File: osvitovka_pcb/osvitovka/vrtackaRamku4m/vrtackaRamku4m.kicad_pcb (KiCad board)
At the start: 2 copper layers, 24 parts, among them J1 Screw_Terminal_01x01, J3 Screw_Terminal_01x01, J5 M+, J6 M-, Q1 BUZ11, SW1 SW_Push, U1 LM78M05_TO220, U2 LTV-817S

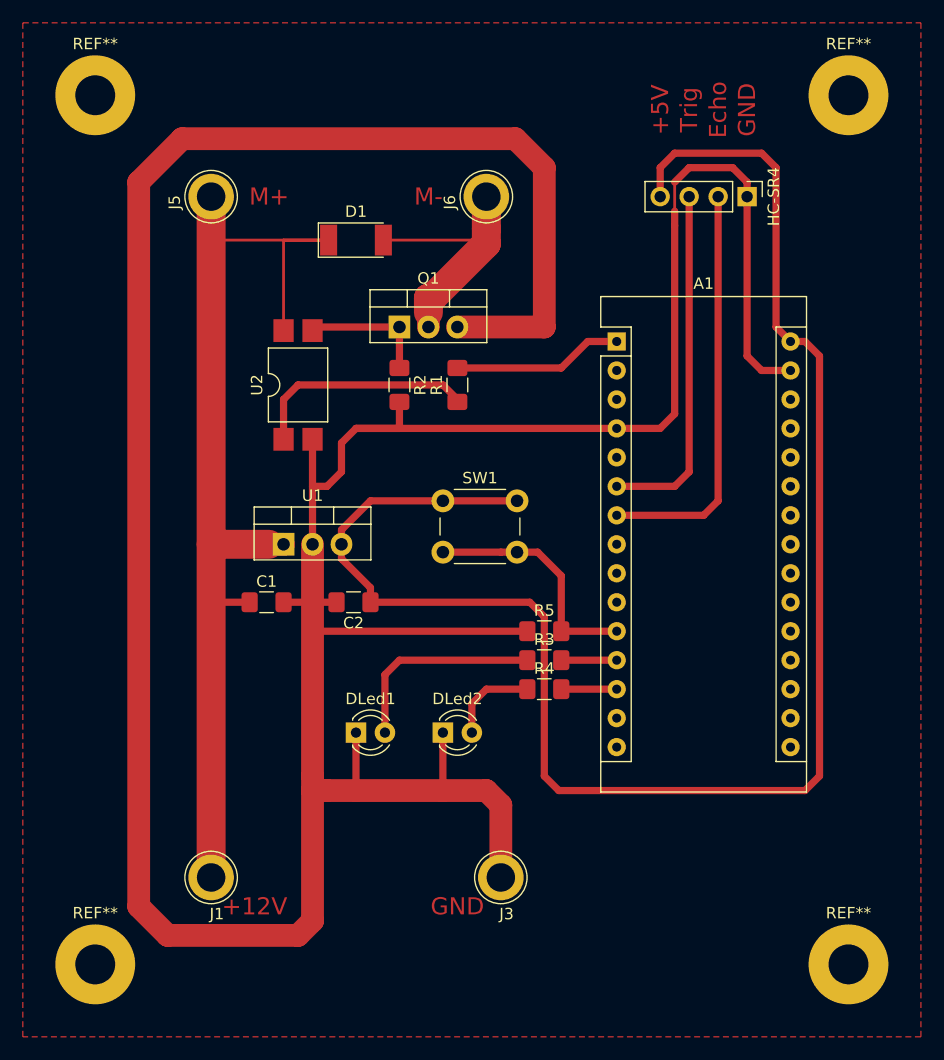
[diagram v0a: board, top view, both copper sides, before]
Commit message: Nová, zmenšená verze.
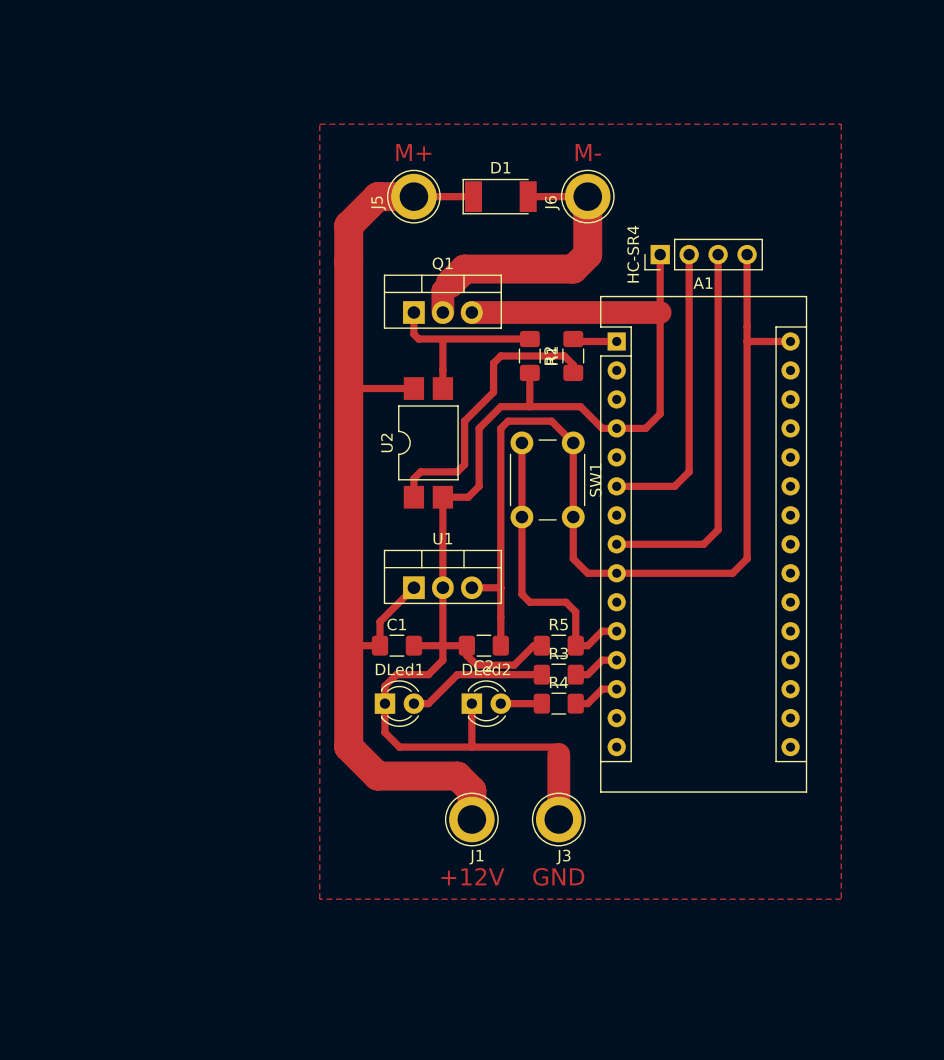
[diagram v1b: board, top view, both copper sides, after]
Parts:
- removed REF** (x4): MountingHole_3.5mm_Pad, MountingHole:MountingHole_3.5mm_Pad
- moved J1 23.4 mm to (141.0, 111.8)
- moved J5 17.8 mm to (135.9, 57.1)
- moved D1 13.3 mm to (143.5, 57.1)
- moved SW1 12.5 mm to (149.9, 78.7), turned to 270 degrees
- moved U2 12.5 mm to (137.2, 78.7)
- moved C1 12.0 mm to (134.4, 96.5)
- moved C2 12.0 mm to (142.0, 96.5)
- moved U1 12.0 mm to (135.9, 91.4)
- moved R2 11.7 mm to (146.1, 71.1)
- moved R1 10.5 mm to (149.9, 71.1)
- moved HC-SR4 9.16 mm to (157.5, 62.2), turned to 90 degrees
- moved J6 8.89 mm to (151.1, 57.1)
- moved J3 7.18 mm to (148.6, 111.8)
- moved DLed1 3.59 mm to (133.3, 101.6)
- moved DLed2 3.59 mm to (141.0, 101.6)
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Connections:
- A1 pad 29: GND -> Net-(A1-Pad29)
- A1 pad 6: Trig -> Echo
- A1 pad 7: Echo -> Net-(A1-Pad7)
- A1 pad 8: Net-(A1-Pad8) -> Trig
- A1 pad 9: Net-(A1-Pad9) -> +5V
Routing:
- net GND: track 354.0 -> 123.5 mm
- net +5V: track 148.2 -> 85.9 mm
- net +12V: track 151.3 -> 130.1 mm
- net PWM1: track 14.9 -> 3.90 mm
- net Echo: track 36.1 -> 25.9 mm
- net Net-(DLed1-Pad2): track 18.4 -> 12.6 mm
- net Net-(Q1-Pad1): track 11.3 -> 16.4 mm
- net Net-(R1-Pad1): track 20.0 -> 24.8 mm
- net Btn1: track 21.0 -> 25.7 mm
- net Net-(DLed2-Pad2): track 8.24 -> 3.90 mm
- net Trig: track 31.0 -> 33.5 mm
- net Net-(D1-Pad2): track 35.5 -> 33.1 mm
- net Led_yellow: track 4.86 -> 4.12 mm
- net Led_green: track 4.86 -> 4.12 mm
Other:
- board text removed: "+5V"
- board text removed: "Echo"
- board text removed: "Trig"

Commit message: Úprava PCB pro jednostranný plošňák.
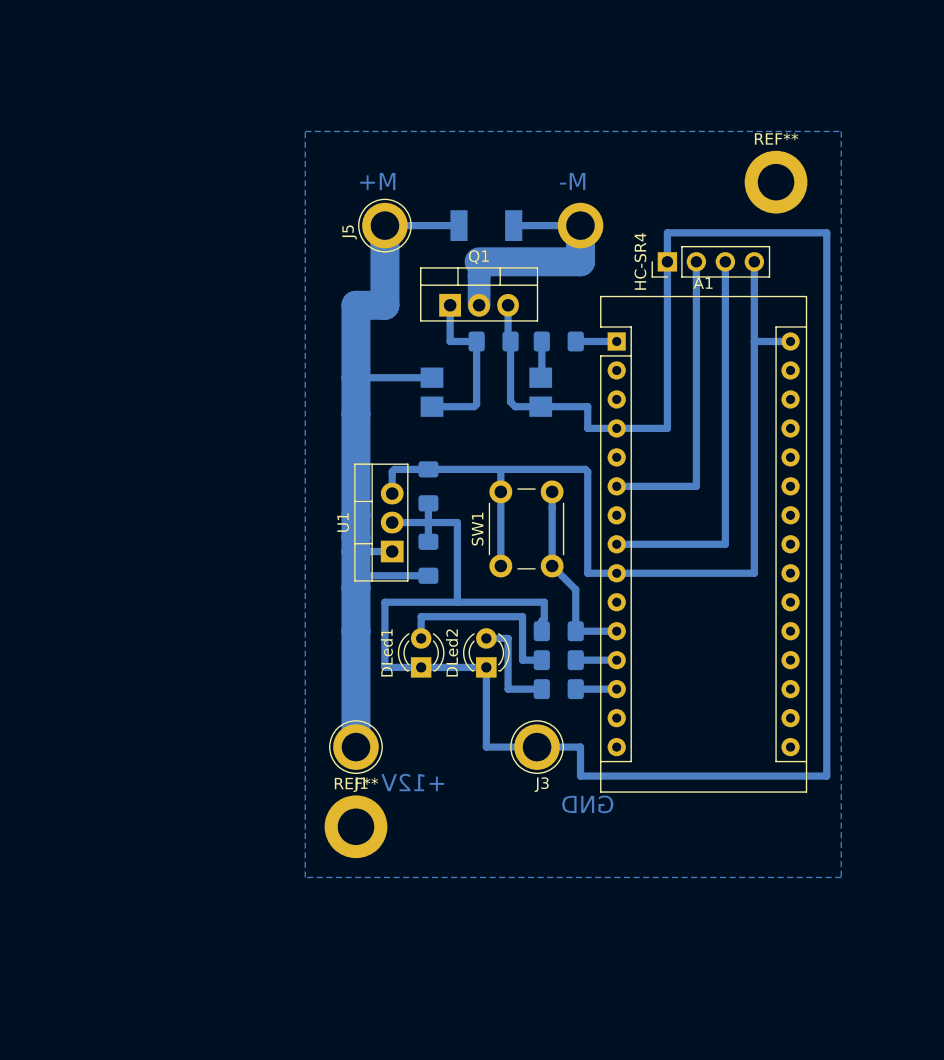
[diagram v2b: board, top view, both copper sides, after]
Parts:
- added REF**: MountingHole_3.2mm_M3_ISO14580_Pad, MountingHole:MountingHole_3.2mm_M3_ISO14580_Pad, F.Cu at (167.6, 55.9)
- added REF**: MountingHole_3.2mm_M3_ISO14580_Pad, MountingHole:MountingHole_3.2mm_M3_ISO14580_Pad, F.Cu at (130.8, 112.4)
- C1, C2, D1, J6, R1, R2, R3, R4, R5, U2: moved to B.Cu
- moved C2 14.8 mm to (137.2, 82.5), turned to 270 degrees
- moved SW1 12.5 mm to (143.5, 89.5), turned to 90 degrees
- moved J1 12.0 mm to (130.8, 105.4)
- moved C1 8.10 mm to (137.2, 88.9), turned to 90 degrees
- moved U2 6.75 mm to (142.2, 74.3), turned to 180 degrees
- moved J3 6.63 mm to (146.7, 105.4)
- moved DLed1 4.49 mm to (136.5, 98.4), turned to 90 degrees
- moved U1 3.70 mm to (134.0, 88.3), turned to 90 degrees
- moved J5 3.59 mm to (133.3, 59.7)
- moved R2 3.42 mm to (142.9, 69.8), turned to 0 degrees
- moved DLed2 3.42 mm to (142.2, 98.4), turned to 90 degrees
- moved Q1 3.24 mm to (139.1, 66.7)
- moved D1 2.84 mm to (142.2, 59.7)
- moved J6 2.62 mm to (150.5, 59.7), turned to 90 degrees
- moved R1 1.80 mm to (148.6, 69.8), turned to 0 degrees
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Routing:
- net GND: track 123.5 -> 189.8 mm
- net +12V: track 130.1 -> 72.3 mm
- net Net-(R1-Pad1): track 24.8 -> 3.22 mm
- net Net-(D1-Pad2): track 33.1 -> 21.7 mm
- net Btn1: track 25.7 -> 16.7 mm
- net Net-(DLed2-Pad2): track 3.90 -> 9.31 mm
- net +5V: track 85.9 -> 81.5 mm
- net Net-(DLed1-Pad2): track 12.6 -> 16.3 mm
- net Net-(Q1-Pad1): track 16.4 -> 15.0 mm
- net Trig: track 33.5 -> 34.3 mm
- net Echo: track 25.9 -> 26.7 mm
- net Led_yellow: track 4.12 -> 3.59 mm
- net Led_green: track 4.12 -> 3.59 mm
- added copper zone on B.Cu, net GND
- removed copper zone on F.Cu, net GND

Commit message: Nový PCB.
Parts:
- removed R5: 10k, Resistor_SMD:R_1206_3216Metric_Pad1.42x1.75mm_HandSolder
- removed REF** (x2): MountingHole_3.2mm_M3_ISO14580_Pad, MountingHole:MountingHole_3.2mm_M3_ISO14580_Pad
- removed SW1: SW_Push, Button_Switch_THT:SW_PUSH_6mm_H5mm
- removed U2: LTV-817S, Package_DIP:SMDIP-4_W9.53mm
- added D2: D, Diode_SMD:D_1206_3216Metric, B.Cu at (138.4, 62.2)
- added H1: MountingHole, MountingHole:MountingHole_3.2mm_M3_ISO14580, F.Cu at (130.8, 111.8)
- added H2: MountingHole, MountingHole:MountingHole_3.2mm_M3_ISO14580, F.Cu at (167.6, 55.9)
- added K1: RSM822, Relay_THT:Relay_DPDT_Finder_40.52, F.Cu at (139.1, 94.0)
- C1, C2: footprint Capacitor_SMD:C_1206_3216Metric_Pad1.42x1.75mm_HandSolder -> Capacitor_THT:C_Disc_D3.0mm_W2.0mm_P2.50mm
- D1: value SM4007 -> D; footprint Diode_SMD:D_MELF -> Diode_SMD:D_1206_3216Metric
- Q1: value BUZ11 -> BC817; footprint Package_TO_SOT_THT:TO-220-3_Vertical -> Package_TO_SOT_SMD:SOT-23; moved to B.Cu
- R1: value 470 -> 4k7; footprint Resistor_SMD:R_1206_3216Metric_Pad1.42x1.75mm_HandSolder -> Resistor_SMD:R_0805_2012Metric
- R2, R3, R4: footprint Resistor_SMD:R_1206_3216Metric_Pad1.42x1.75mm_HandSolder -> Resistor_SMD:R_0805_2012Metric
- moved D1 37.5 mm to (142.9, 97.2), turned to 180 degrees
- moved C2 22.2 mm to (132.1, 104.1), turned to 90 degrees
- moved Q1 21.6 mm to (139.7, 88.3), turned to 180 degrees
- moved R1 18.7 mm to (145.4, 88.3), turned to 270 degrees
- moved R2 18.4 mm to (142.9, 88.3), turned to 90 degrees
- moved J1 10.9 mm to (139.7, 111.8)
- moved R4 10.5 mm to (138.1, 100.3)
- moved DLed1 9.94 mm to (145.4, 102.9), turned to 0 degrees
- moved U1 8.47 mm to (132.1, 96.5)
- moved J2 6.48 mm to (148.0, 111.8)
- moved J4 6.25 mm to (144.8, 62.2), turned to 0 degrees
- moved C1 5.68 mm to (132.1, 86.4)
- moved DLed2 5.12 mm to (139.7, 102.9), turned to 180 degrees
- moved J3 2.84 mm to (132.1, 62.2), turned to 180 degrees
- moved R3 2.29 mm to (150.5, 99.1)
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- renumbered HC-SR4 to HC-SR1, J3 to J2, J5 to J3, J6 to J4
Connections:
- A1 pad 1: PWM1 -> Net-(A1-Pad1)
- A1 pad 10: Net-(A1-Pad10) -> PWM1
- A1 pad 11: Btn1 -> Net-(A1-Pad11)
- A1 pad 13: Led_green -> Net-(A1-Pad13)
- A1 pad 9: +5V -> Net-(A1-Pad9)
- J3 pad 1: +12V -> Net-(D2-Pad1)
- J4 pad 1: Net-(D1-Pad2) -> GND
- Q1 pad 2: Net-(D1-Pad2) -> GND
- Q1 pad 3: GND -> Net-(D1-Pad2)
- R1 pad 1: Net-(R1-Pad1) -> Net-(Q1-Pad1)
- R2 pad 1: Net-(Q1-Pad1) -> GND
- R2 pad 2: GND -> Net-(Q1-Pad1)
- R4 pad 2: Led_green -> +5V
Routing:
- net +12V: track 72.3 -> 105.0 mm, vias 0 -> 2
- net Net-(D2-Pad1): track 0.00 -> 25.2 mm
- net GND: track 189.8 -> 212.8 mm
- net Btn1: track 16.7 -> 0.00 mm
- net +5V: track 81.5 -> 95.6 mm
- net Net-(DLed1-Pad2): track 16.3 -> 4.47 mm
- net Net-(D1-Pad2): track 21.7 -> 11.1 mm
- net Net-(Q1-Pad1): track 15.0 -> 4.74 mm
- net PWM1: track 3.59 -> 11.9 mm
- net Net-(DLed2-Pad2): track 9.31 -> 2.54 mm
- net Led_green: track 3.59 -> 0.00 mm
- net Net-(R1-Pad1): track 3.22 -> 0.00 mm
- net Led_yellow: track 3.59 -> 2.24 mm
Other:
- board text removed: "+12V"
- board text removed: "GND"
- board text removed: "M+"
- board text removed: "M-"

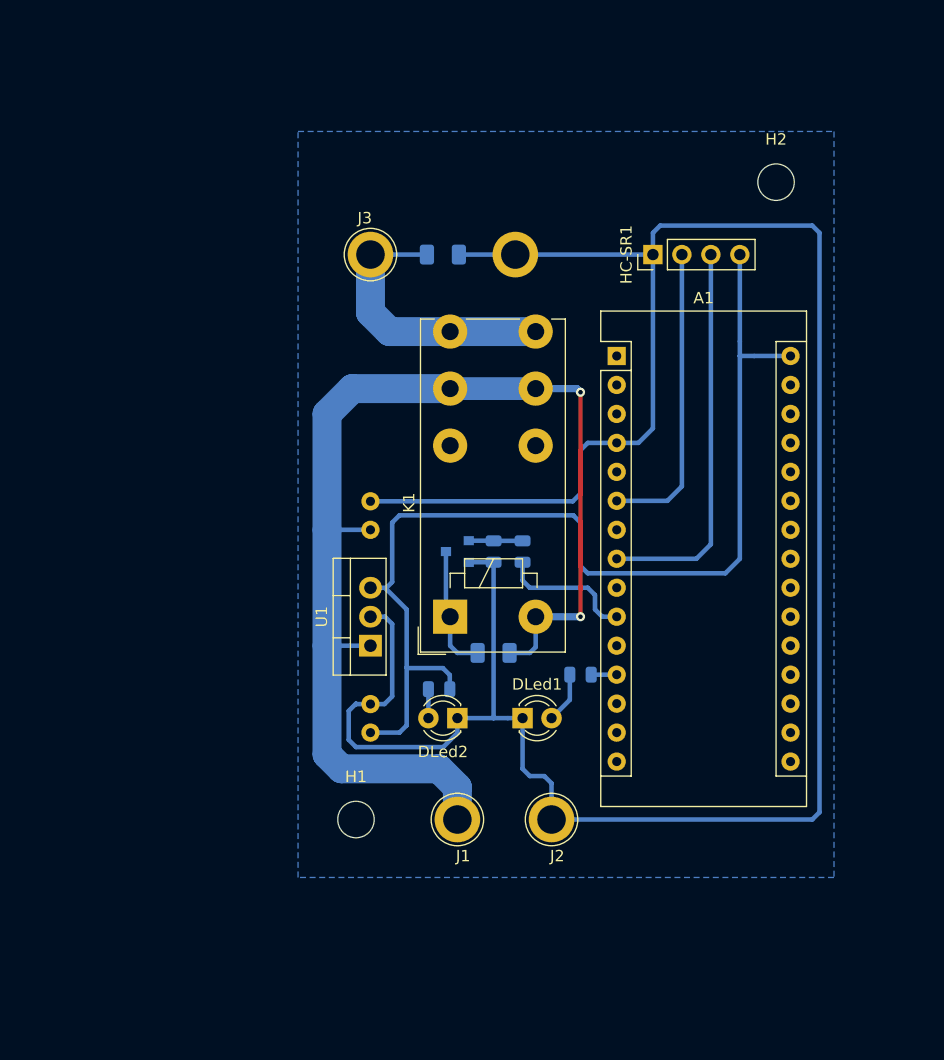
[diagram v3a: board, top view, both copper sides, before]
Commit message: Měl jsem špatný pouzdro na relátku. Opraveno.
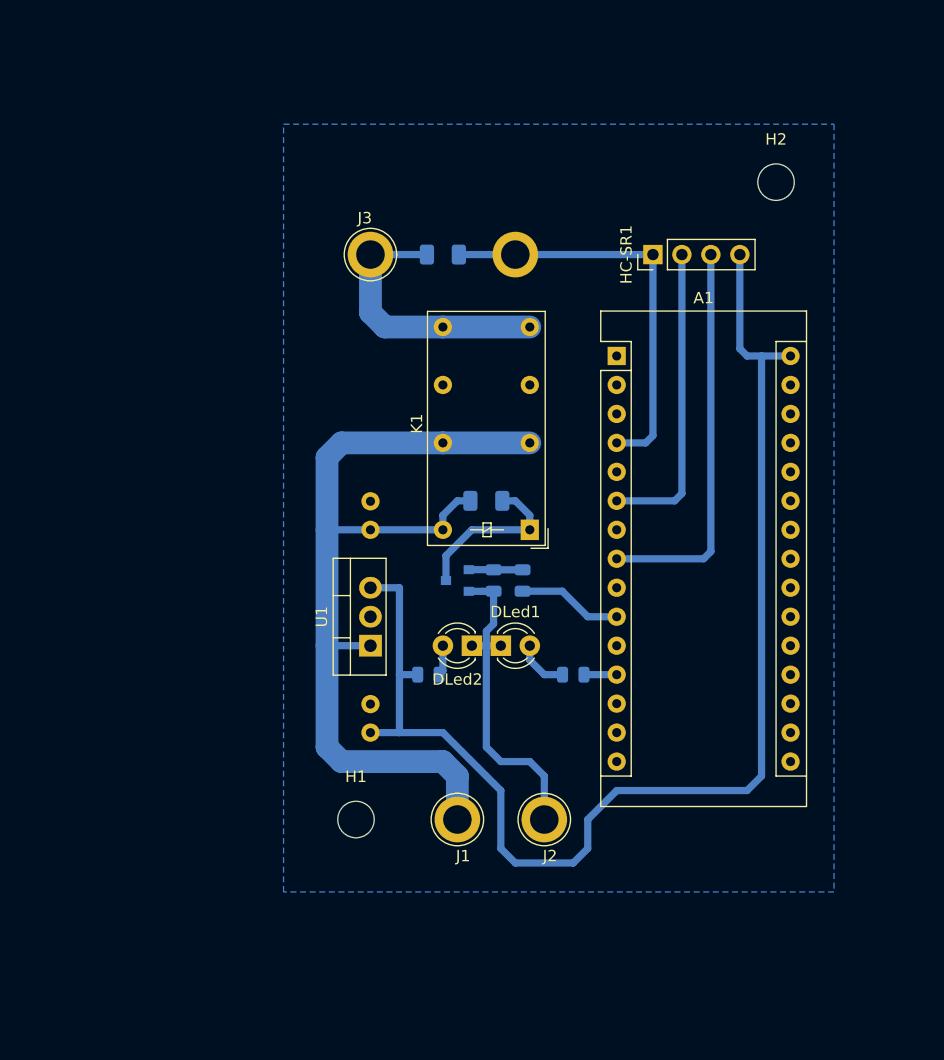
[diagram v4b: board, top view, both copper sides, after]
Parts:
- K1: footprint Relay_THT:Relay_DPDT_Finder_40.52 -> Relay_THT:Relay_DPDT_Finder_30.22
- moved D1 13.4 mm to (142.2, 83.8), turned to 0 degrees
- moved K1 10.3 mm to (146.1, 86.4)
- moved DLed1 6.63 mm to (143.5, 96.5)
- moved DLed2 6.48 mm to (141.0, 96.5)
- moved Q1 2.54 mm to (139.7, 90.8)
- moved R1 2.54 mm to (145.4, 90.8)
- moved R2 2.54 mm to (142.9, 90.8)
- moved R4 1.58 mm to (137.2, 99.1), turned to 180 degrees
- moved J2 0.64 mm to (147.3, 111.8)
- moved R3 0.63 mm to (149.9, 99.1)
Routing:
- net GND: track 212.8 -> 64.9 mm
- net +12V: track 105.0 -> 78.2 mm, vias 2 -> 0
- net +5V: track 95.6 -> 113.3 mm
- net Net-(D1-Pad2): track 11.1 -> 14.7 mm
- net PWM1: track 11.9 -> 9.18 mm
- net Net-(D2-Pad1): track 25.2 -> 24.5 mm
- net Led_yellow: track 2.24 -> 2.87 mm

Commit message: test a upgrade pcb.
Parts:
- D1, D2: footprint Diode_SMD:D_1206_3216Metric -> Diode_SMD:D_1806_4516Metric_Pad1.57x1.80mm_HandSolder
- moved C2 47.1 mm to (165.6, 71.1), turned to 270 degrees
- moved U1 35.6 mm to (165.6, 84.6), turned to 270 degrees
- moved C1 34.2 mm to (165.6, 79.5)
- moved R4 29.1 mm to (165.9, 94.0)
- moved DLed2 24.8 mm to (165.6, 99.6), turned to 90 degrees
- moved J2 20.7 mm to (168.0, 113.0)
- moved D1 8.32 mm to (134.1, 82.0)
- moved K1 8.19 mm to (137.9, 85.3)
- moved R3 8.13 mm to (141.7, 99.1)
- moved A1 8.13 mm to (145.5, 71.1)
- moved DLed1 8.03 mm to (135.9, 99.1)
- moved HC-SR1 6.98 mm to (149.9, 62.2)
- moved R2 6.32 mm to (137.4, 94.0), turned to 0 degrees
- moved J3 5.27 mm to (130.7, 57.1)
- moved D2 5.09 mm to (138.0, 57.1)
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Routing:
- net GND: track 64.9 -> 179.0 mm
- net +5V: track 113.3 -> 43.4 mm
- net +12V: track 78.2 -> 113.9 mm
- net Net-(D1-Pad2): track 14.7 -> 8.00 mm
- net PWM1: track 9.18 -> 2.87 mm
- net Net-(DLed1-Pad2): track 4.67 -> 2.36 mm
- net Net-(DLed2-Pad2): track 2.68 -> 4.01 mm
- net Net-(D2-Pad1): track 24.5 -> 23.5 mm
- net Net-(Q1-Pad1): track 4.74 -> 5.33 mm
